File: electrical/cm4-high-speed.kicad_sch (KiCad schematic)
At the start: 1 part

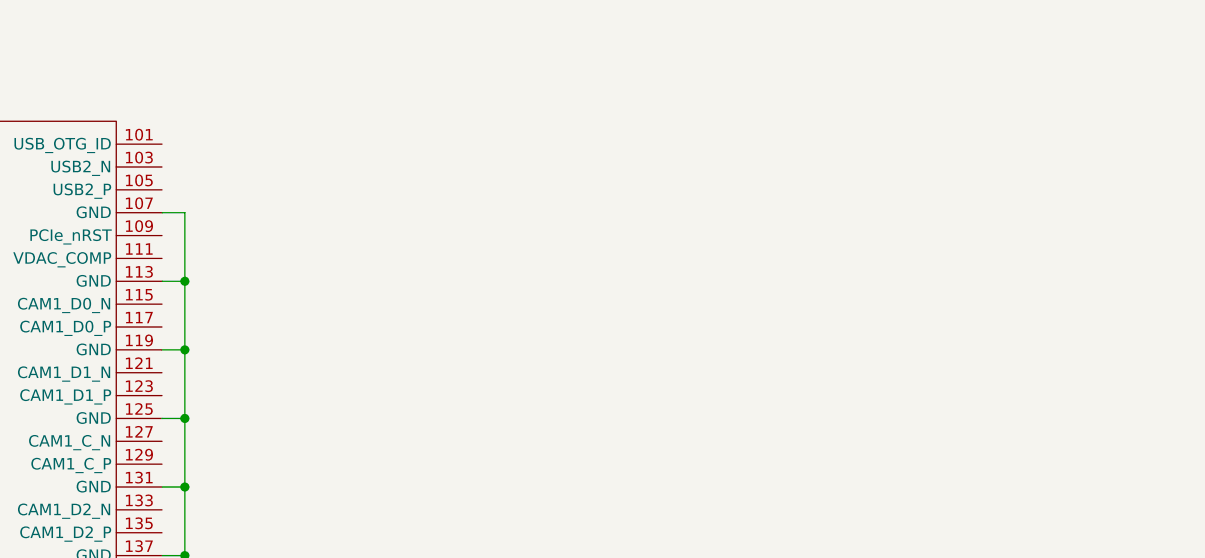
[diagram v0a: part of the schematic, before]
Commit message: Micro B + Header for eMMC flash
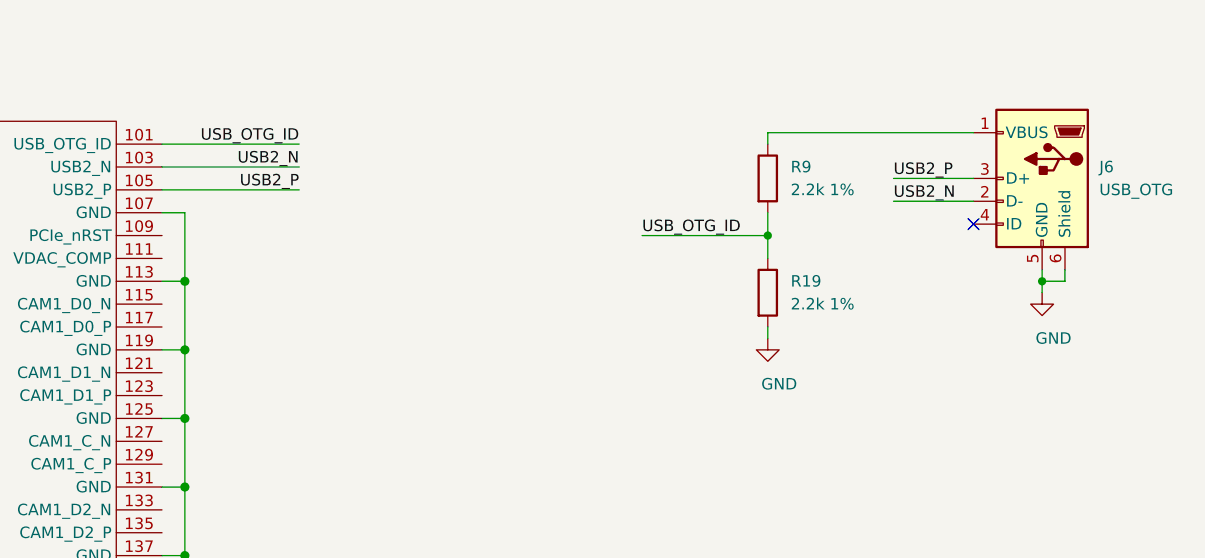
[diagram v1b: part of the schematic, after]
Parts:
- added J6: USB_OTG, symbol Connector:USB_OTG
- added R19, R9: 2.2k 1%, symbol Device:R
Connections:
- net GND: now also J6.5 (GND), J6.6 (Shield), R19.2
- net USB_OTG_ID: now reaches Module1.101 (USB_OTG_ID)
- net USB_OTG_ID: now also R19.1, R9.2
- net USB2_N: now reaches Module1.103 (USB2_N)
- net USB2_N: now also J6.2 (D-)
- net USB2_P: now reaches Module1.105 (USB2_P)
- net USB2_P: now also J6.3 (D+)
- new net: J6.1 (VBUS), R9.1
- no-connect marks 0 -> 1
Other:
- title: Raspberry Pi Compute Module 4 Carrier Template -> Network Tap
